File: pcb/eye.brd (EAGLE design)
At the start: 158.8 x 54 mm, 91 parts, among them Q1 ECS-160-20-3X-TR, U1 WS2812, U10 WS2812, U11 WS2812, U12 WS2812, U13 WS2812, U14 WS2812, U15 WS2812, U16 WS2812, U17 WS2812, U18 WS2812, U19 WS2812, U2 WS2812, U20 WS2812, U21 WS2812, U22 WS2812, U23 WS2812, U24 WS2812, U25 WS2812, U26 WS2812, U27 WS2812, U28 WS2812, U29 WS2812, U3 WS2812, U30 WS2812, U31 WS2812, U32 WS2812, U33 WS2812, U34 WS2812, U35 WS2812, U36 WS2812, U37 WS2812, U38 WS2812, U39 WS2812, U4 WS2812, U40 WS2812, U41 WS2812, U42 WS2812, U43 WS2812, U44 WS2812, U45 WS2812, U46 WS2812, U47 WS2812, U48 WS2812, U49 WS2812, U5 WS2812, U50 WS2812, U51 WS2812, U52 WS2812, U53 WS2812, U54 WS2812, U55 WS2812, U56 WS2812, U57 WS2812, U58 WS2812, U59 WS2812, U6 WS2812, U60 WS2812, U7 WS2812, U8 WS2812, U9 WS2812

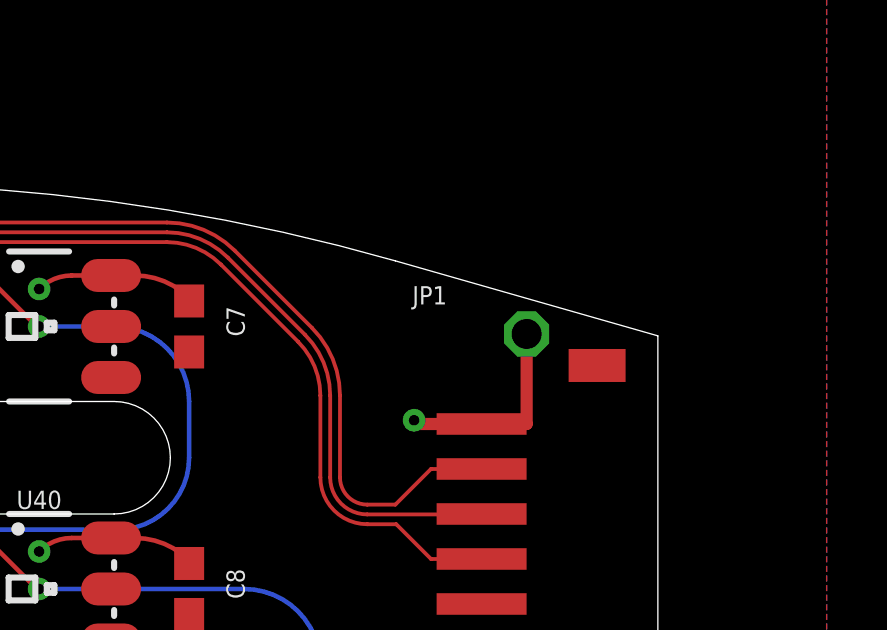
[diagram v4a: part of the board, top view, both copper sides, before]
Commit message: update values and name placement
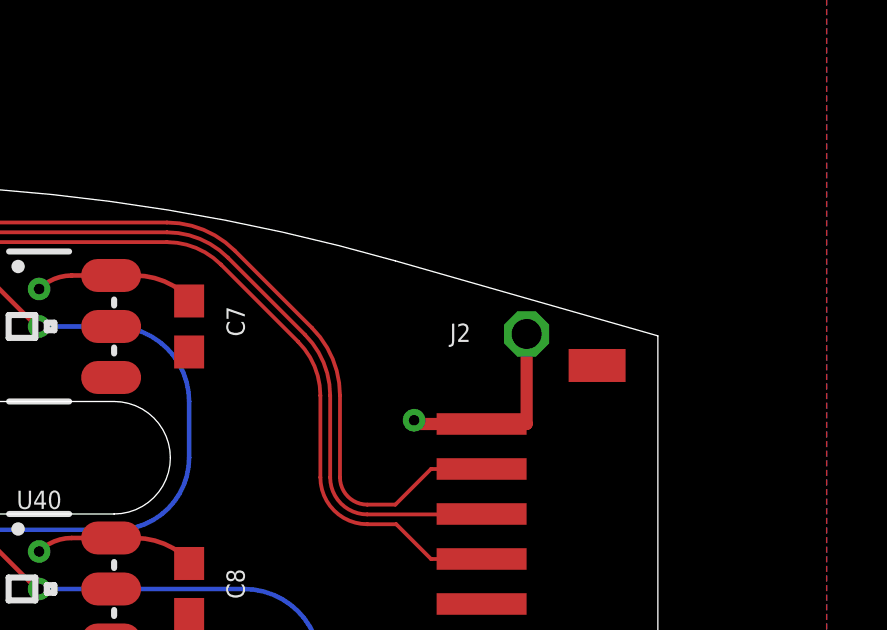
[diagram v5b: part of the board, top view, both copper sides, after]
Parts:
- renumbered JP1 to J2
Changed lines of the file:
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@@
 <setting verticaltext="up"/>
 </settings>
-<grid distance="2.5" unitdist="mm" unit="mm" style="lines" multiple="1" display="yes" altdistance="5" altunitdist="mil" altunit="mil"/>
+<grid distance="0.625" unitdist="mm" unit="mm" style="lines" multiple="1" display="yes" altdistance="5" altunitdist="mil" altunit="mil"/>
 <layers>
 <layer number="1" name="Top" color="4" fill="1" visible="yes" active="yes"/>
@@
 <attribute name="VALUE" x="76.407896875" y="38.907896875" size="0.6096" layer="27" font="vector" ratio="20" rot="R315" align="bottom-center"/>
 </element>
-<element name="JP1" library="josh" package="JST-ZH-5-SMD-RA" value="JST-ZH-5SMD-RA" x="155" y="46.25" smashed="yes" rot="R270">
-<attribute name="NAME" x="151.19" y="53.235" size="0.6096" layer="25" ratio="10"/>
+<element name="J2" library="josh" package="JST-ZH-5-SMD-RA" value="JST-ZH-5SMD-RA" x="155" y="46.25" smashed="yes" rot="R270">
+<attribute name="NAME" x="152.44" y="51.985" size="0.6096" layer="25" ratio="10"/>
 <attribute name="VALUE" x="151.19" y="37.995" size="1.27" layer="27"/>
 </element>
@@
 <wire x1="5.35" y1="47.55" x2="7.1375" y2="47.55" width="0.4064" layer="1"/>
 <wire x1="7.1375" y1="47.55" x2="7.1875" y2="47.5" width="0.508" layer="1" curve="-90"/>
-<contactref element="JP1" pad="P$1"/>
+<contactref element="J2" pad="P$1"/>
 <via x="85.625" y="46.5625" extent="1-16" drill="0.35"/>
 <via x="83.4375" y="48.75" extent="1-16" drill="0.35"/>
@@
 <wire x1="2.625" y1="46.25" x2="2.625" y2="44.375" width="0.4064" layer="1"/>
 <wire x1="2.625" y1="44.375" x2="2.625" y2="42.565" width="0.4064" layer="1"/>
-<contactref element="JP1" pad="P$5"/>
+<contactref element="J2" pad="P$5"/>
 <contactref element="U$5" pad="P$1"/>
 <contactref element="U$5" pad="P$2"/>
@@
 <signal name="N$30">
 <contactref element="32U4" pad="41"/>
-<contactref element="JP1" pad="P$4"/>
+<contactref element="J2" pad="P$4"/>
 <wire x1="81.69705625" y1="45.61126875" x2="82.29556875" y2="46.20978125" width="0.127" layer="1"/>
 <wire x1="82.29556875" y1="46.20978125" x2="82.54023125" y2="46.20978125" width="0.127" layer="1"/>
@@
 <signal name="N$63">
 <contactref element="32U4" pad="40"/>
-<contactref element="JP1" pad="P$3"/>
+<contactref element="J2" pad="P$3"/>
 <wire x1="82.050609375" y1="45.257715625" x2="82.77145" y2="45.97855625" width="0.127" layer="1"/>
 <wire x1="82.77145" y1="45.97855625" x2="82.77145625" y2="45.97855625" width="0.127" layer="1"/>
@@
 <signal name="N$64">
 <contactref element="32U4" pad="39"/>
-<contactref element="JP1" pad="P$2"/>
+<contactref element="J2" pad="P$2"/>
 <wire x1="82.4041625" y1="44.9041625" x2="83.00268125" y2="45.50268125" width="0.127" layer="1"/>
 <wire x1="83.00268125" y1="45.50268125" x2="83.00268125" y2="45.74733125" width="0.127" layer="1"/>

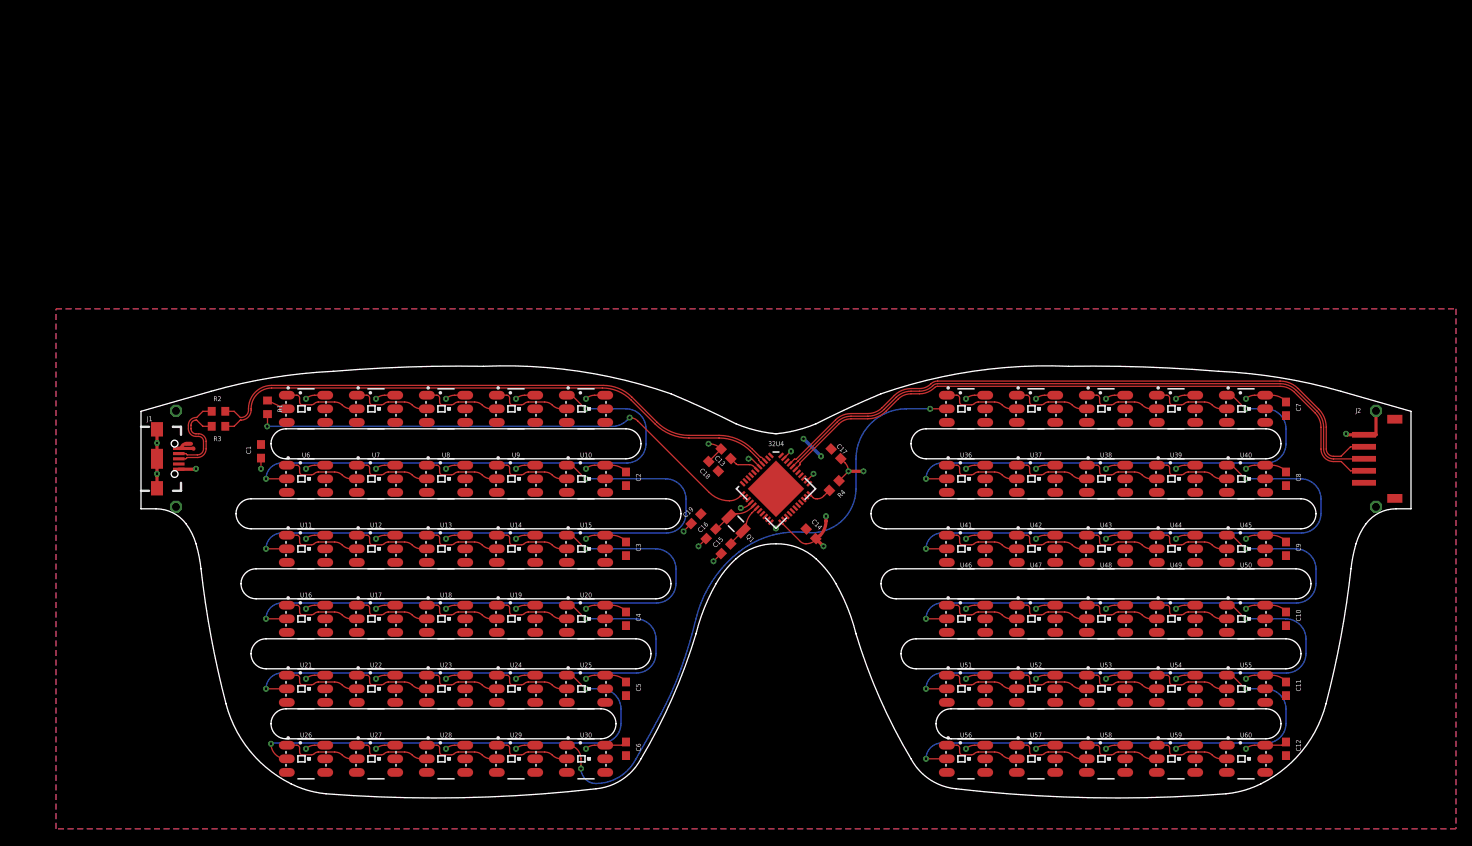
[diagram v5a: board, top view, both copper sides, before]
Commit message: touch up silkscreen and traces
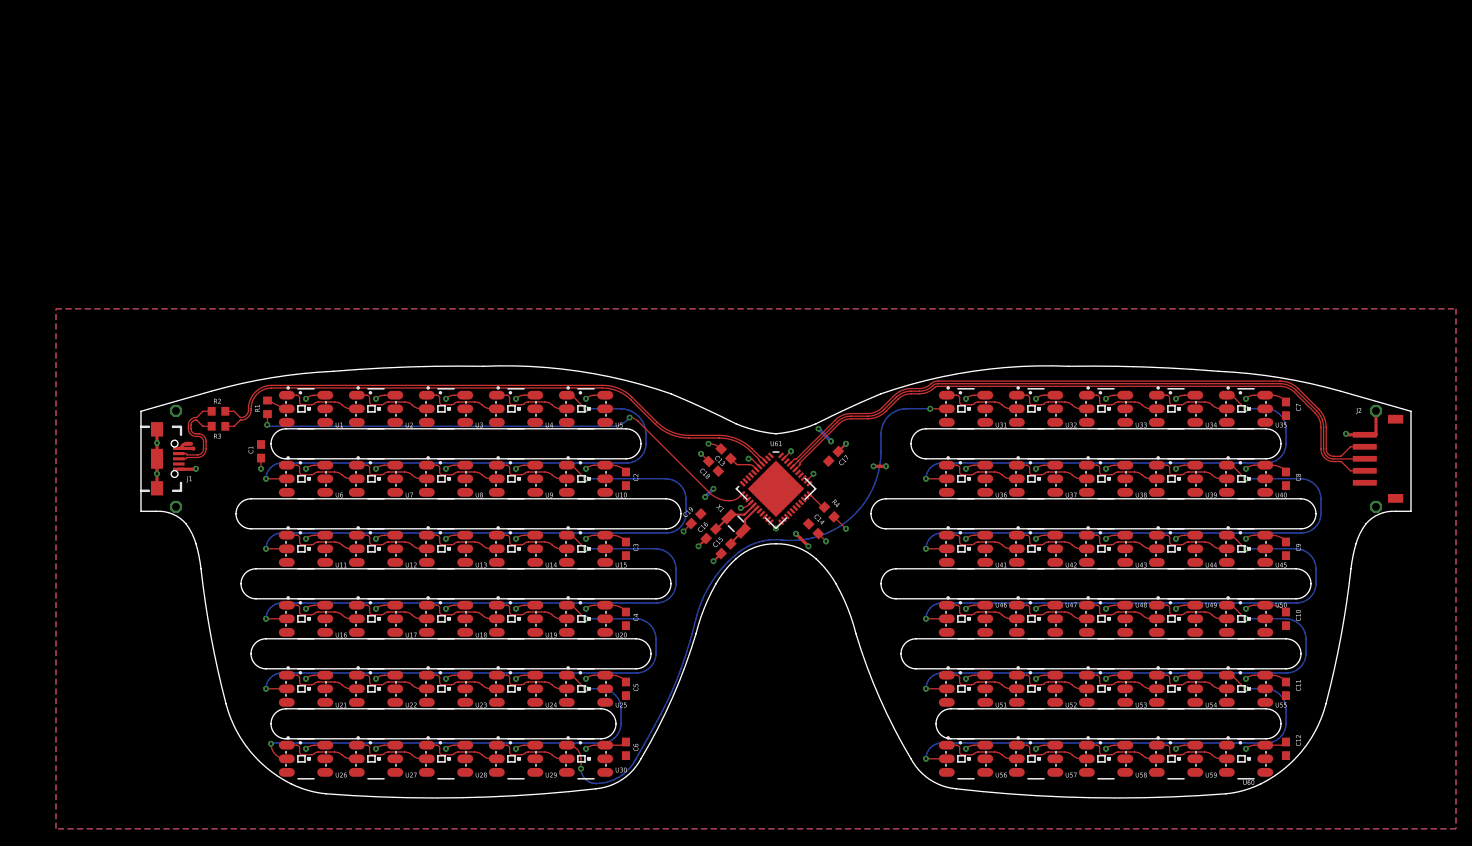
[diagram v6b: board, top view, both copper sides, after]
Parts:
- moved R4 3.37 mm to (86.7, 39.6), turned to 135 degrees
- moved C14 0.70 mm to (84.7, 37.5)
- moved U$1 0.62 mm to (80.0, 38.1)
- moved C17 0.44 mm to (87.2, 46.6), turned to 45 degrees
- moved J2 0.10 mm to (155.1, 46.2)
- renumbered 32U4 to U61, Q1 to X1
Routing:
- net GND: track 228.6 -> 220.8 mm, vias 78 -> 82
- net N$60: track 76.0 -> 75.2 mm
- net +5V: track 7.40 -> 7.98 mm, vias 2 -> 4
- net N$77: track 3.10 -> 2.57 mm
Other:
- outline, holes or cut-outs redrawn
- board text added: "github.com/joshuaboud/pixel_eyes"

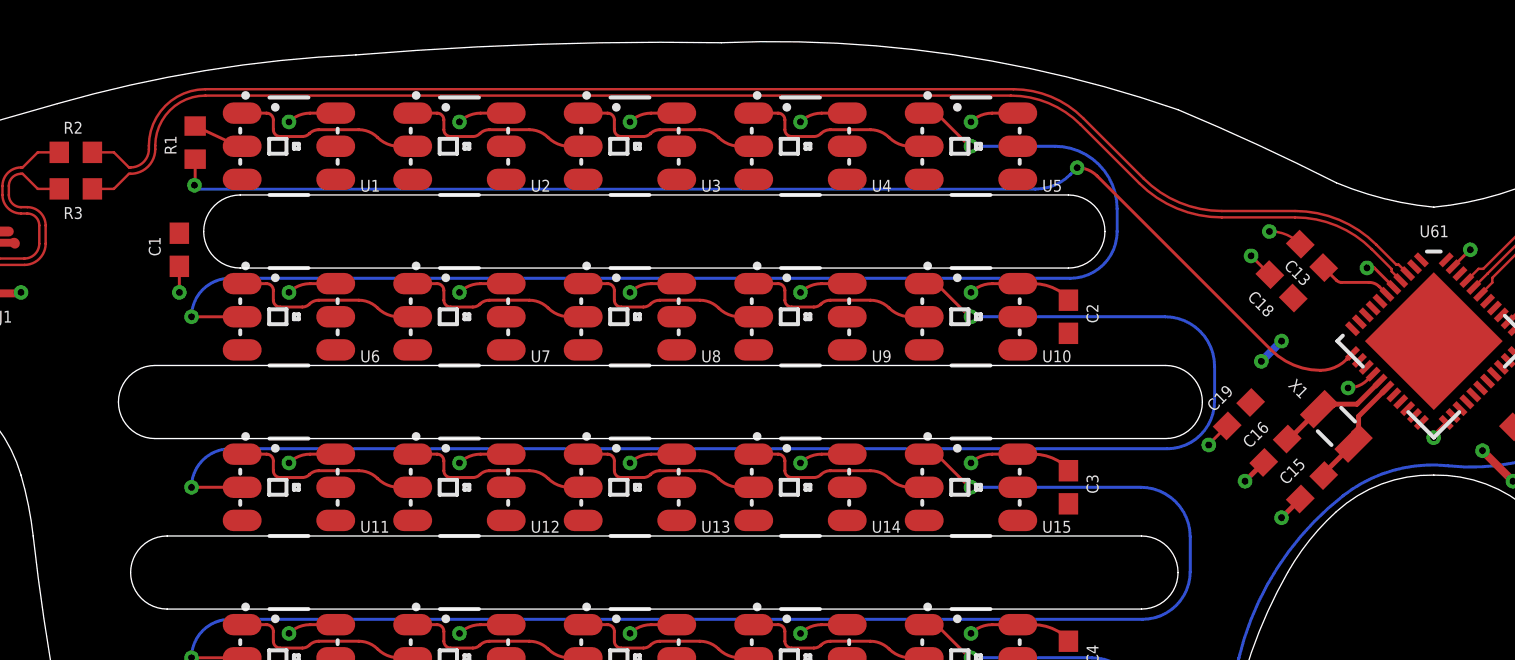
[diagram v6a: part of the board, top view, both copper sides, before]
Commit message: add avr-isp header to glasses
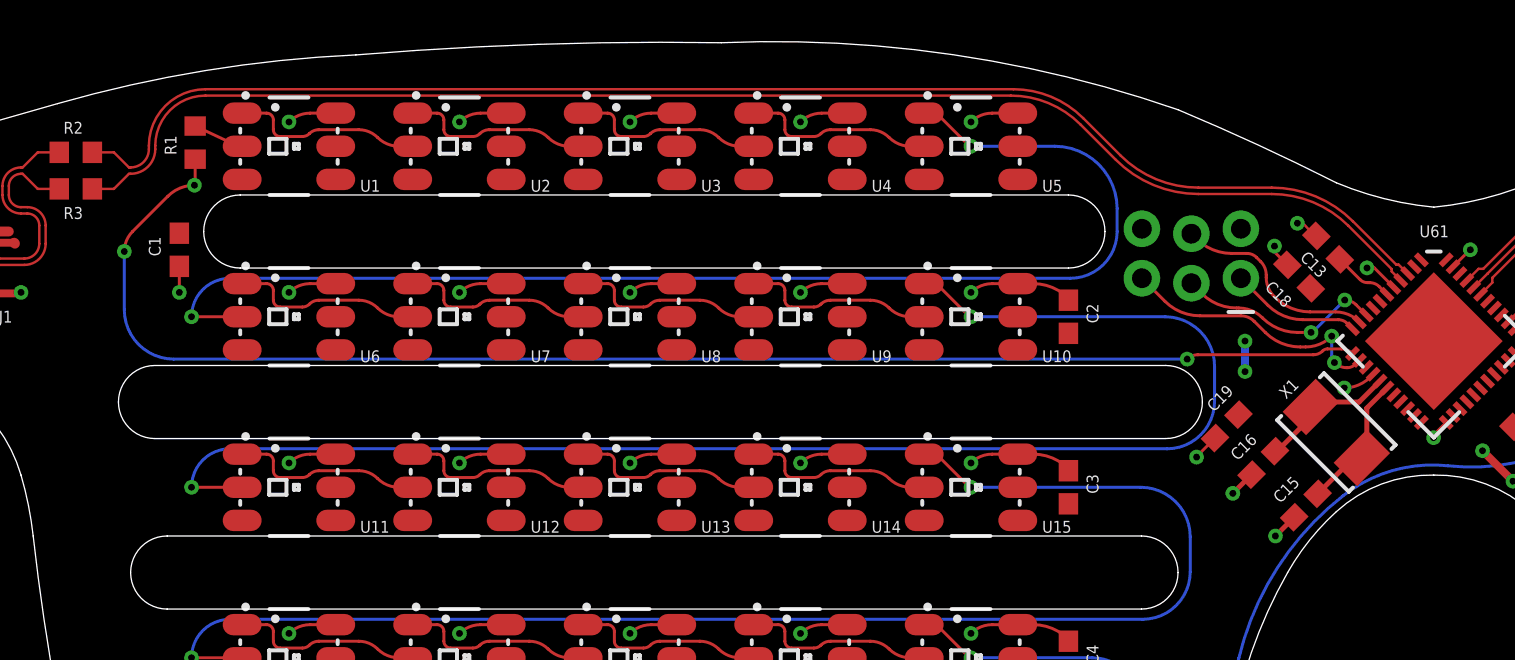
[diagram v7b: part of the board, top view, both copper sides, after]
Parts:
- added J3: AVR_SPI_PROG_3X22X3_LOCK, SparkFun-Connectors:2X3_LOCK
- X1: device SparkFun-Clocks:CRYSTAL-SMD-3.2X1.5MM -> SparkFun-Clocks:CRYSTAL-SMD-5X3.2-2PAD
- moved C18 1.03 mm to (73.1, 45.8)
- moved C15 0.99 mm to (73.4, 34.1)
- moved C13 0.93 mm to (74.6, 47.3)
- moved C16 0.88 mm to (71.2, 36.2)
- moved C19 0.88 mm to (69.4, 38.1)
- moved X1 0.31 mm to (75.0, 37.8), turned to 315 degrees
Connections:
- new net N$65: J3.1, U61.11
- new net N$66: J3.4, U61.10
- new net N$69: J3.3, U61.9
- net +5V: now also J3.2
- net GND: now also J3.6
- net RST: now also J3.5
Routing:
- net RST: track 0.00 -> 13.8 mm, vias 0 -> 2
- net N$69: track 0.00 -> 10.5 mm, vias 0 -> 2
- net N$66: track 0.00 -> 10.5 mm
- net LED_DATA: track 65.4 -> 73.9 mm, vias 2 -> 3
- net N$65: track 0.00 -> 6.60 mm
- net N$68: track 6.02 -> 7.45 mm
- net N$67: track 6.02 -> 7.17 mm
- net N$62: track 3.74 -> 3.09 mm
